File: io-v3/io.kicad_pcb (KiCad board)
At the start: 2 copper layers, 99 parts, among them P1 OUT_GND, P10 INJ-CPU, P11 INJECTORS, P12 LSD-CPU, P13 LSDS, P2 TRIG-cpu, P3 DIG-CPU, P4 IN-CPU, P5 CPU_PWR, P6 TRIG-IN, P7 DIG-IN, P8 IGNITION, P9 PWR_IN, Q1 MOSFET, Q2 MOSFET, Q3 MOSFET, Q4 MOSFET, Q5 MOSFET, Q6 MOSFET, Q7 MOSFET, Q8 MOSFET, U1 LM2940, U12 MIC4469, U13 MIC4469, U2 MIC4469, U3 MAX9926UAEE+

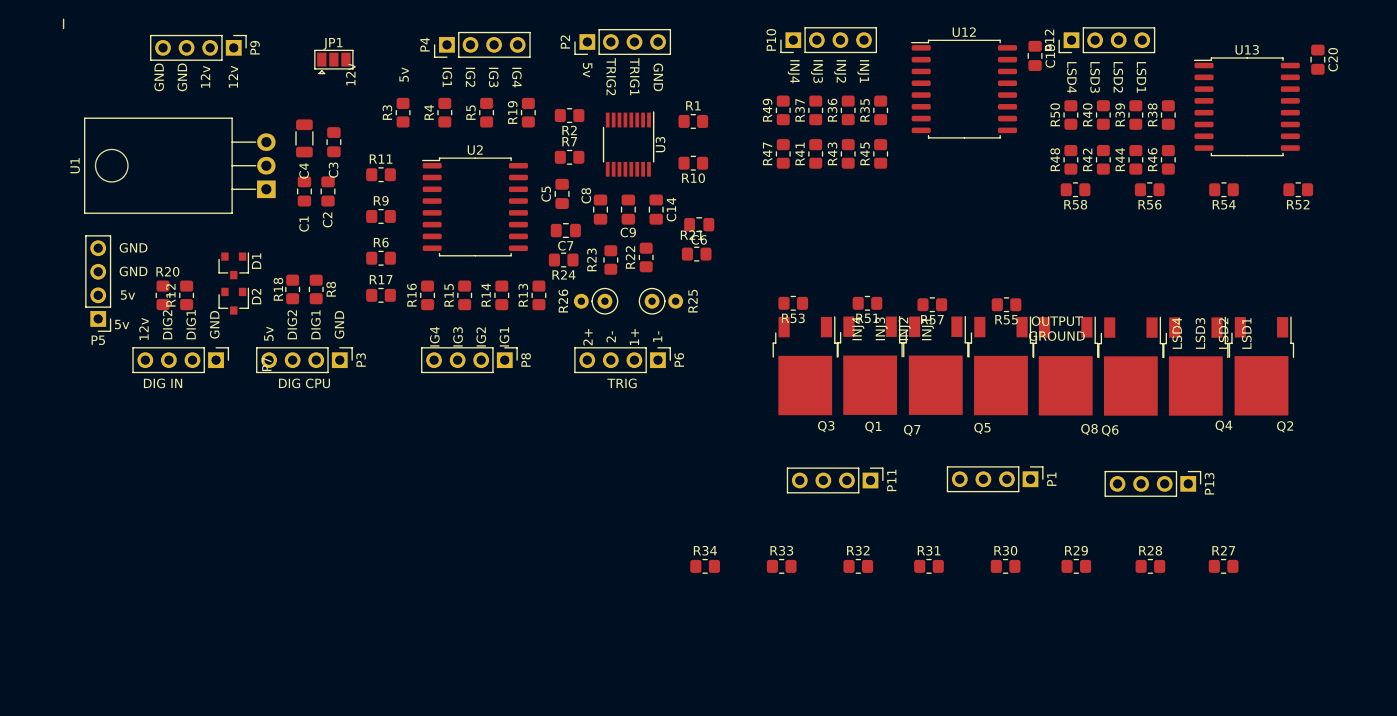
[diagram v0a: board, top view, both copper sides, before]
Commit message: Add LEDs and make a board size
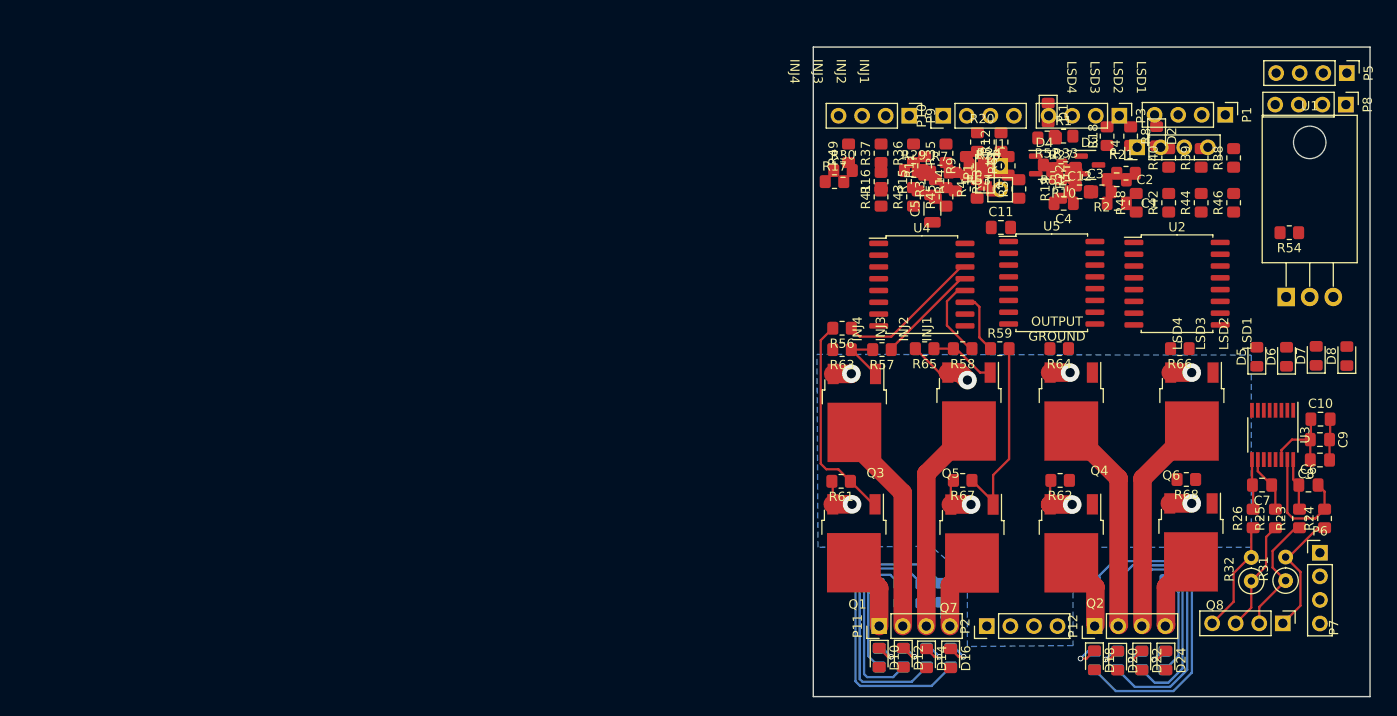
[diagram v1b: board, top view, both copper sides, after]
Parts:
- removed C14: 1u, Capacitor_SMD:C_0805_2012Metric_Pad1.18x1.45mm_HandSolder
- removed C19, C20: 1 uF, Capacitor_SMD:C_0805_2012Metric_Pad1.18x1.45mm_HandSolder
- removed P13: LSDS, Connector_PinHeader_2.54mm:PinHeader_1x04_P2.54mm_Vertical
- removed U12, U13: MIC4469, Package_SO:SOIC-16W_7.5x10.3mm_P1.27mm
- added C10: 1u, Capacitor_SMD:C_0805_2012Metric_Pad1.18x1.45mm_HandSolder, F.Cu at (170.5, 148.6)
- added C11: 1 uF, Capacitor_SMD:C_0805_2012Metric_Pad1.18x1.45mm_HandSolder, F.Cu at (136.0, 127.9)
- added C12: 1 uF, Capacitor_SMD:C_0805_2012Metric_Pad1.18x1.45mm_HandSolder, F.Cu at (144.5, 124.1)
- added D10: LED, LED_SMD:LED_0805_2012Metric_Pad1.15x1.40mm_HandSolder, F.Cu at (122.9, 174.3)
- added D11: 1N4148, Diode_SMD:D_0805_2012Metric_Pad1.15x1.40mm_HandSolder, B.Cu at (125.1, 167.4)
- added D12: LED, LED_SMD:LED_0805_2012Metric_Pad1.15x1.40mm_HandSolder, F.Cu at (125.5, 174.3)
- added D13: 1N4148, Diode_SMD:D_0805_2012Metric_Pad1.15x1.40mm_HandSolder, B.Cu at (127.5, 167.4)
- added D14: LED, LED_SMD:LED_0805_2012Metric_Pad1.15x1.40mm_HandSolder, F.Cu at (128.0, 174.4)
- added D15: 1N4148, Diode_SMD:D_0805_2012Metric_Pad1.15x1.40mm_HandSolder, B.Cu at (129.6, 167.3)
- added D16: LED, LED_SMD:LED_0805_2012Metric_Pad1.15x1.40mm_HandSolder, F.Cu at (130.6, 174.4)
- added D17: 1N4148, Diode_SMD:D_0805_2012Metric_Pad1.15x1.40mm_HandSolder, B.Cu at (146.1, 167.0)
- added D18: LED, LED_SMD:LED_0805_2012Metric_Pad1.15x1.40mm_HandSolder, F.Cu at (146.1, 174.6)
- added D19: 1N4148, Diode_SMD:D_0805_2012Metric_Pad1.15x1.40mm_HandSolder, B.Cu at (148.6, 167.0)
- added D20: LED, LED_SMD:LED_0805_2012Metric_Pad1.15x1.40mm_HandSolder, F.Cu at (148.6, 174.6)
- added D21: 1N4148, Diode_SMD:D_0805_2012Metric_Pad1.15x1.40mm_HandSolder, B.Cu at (151.2, 166.9)
- added D22: LED, LED_SMD:LED_0805_2012Metric_Pad1.15x1.40mm_HandSolder, F.Cu at (151.2, 174.6)
- added D23: 1N4148, Diode_SMD:D_0805_2012Metric_Pad1.15x1.40mm_HandSolder, B.Cu at (153.8, 166.9)
- added D24: LED, LED_SMD:LED_0805_2012Metric_Pad1.15x1.40mm_HandSolder, F.Cu at (153.8, 174.6)
- added D3: BAT54S, Package_TO_SOT_SMD:SOT-23, F.Cu at (145.6, 121.2)
- added D4: BAT54S, Package_TO_SOT_SMD:SOT-23, F.Cu at (140.7, 121.2)
- added D5: LED, LED_SMD:LED_0805_2012Metric_Pad1.15x1.40mm_HandSolder, F.Cu at (163.6, 141.9)
- added D6: LED, LED_SMD:LED_0805_2012Metric_Pad1.15x1.40mm_HandSolder, F.Cu at (166.8, 141.9)
- added D7: LED, LED_SMD:LED_0805_2012Metric_Pad1.15x1.40mm_HandSolder, F.Cu at (170.0, 141.8)
- added D8: LED, LED_SMD:LED_0805_2012Metric_Pad1.15x1.40mm_HandSolder, F.Cu at (173.3, 141.8)
- added D9: 1N4148, Diode_SMD:D_0805_2012Metric_Pad1.15x1.40mm_HandSolder, B.Cu at (122.8, 167.3)
- added J1: DIG-in, Connector_PinHeader_2.54mm:PinHeader_1x02_P2.54mm_Vertical, F.Cu at (135.9, 121.3)
- added R59: 150, Resistor_SMD:R_0805_2012Metric_Pad1.20x1.40mm_HandSolder, F.Cu at (135.9, 141.0)
- added R60: 1k, Resistor_SMD:R_0805_2012Metric_Pad1.20x1.40mm_HandSolder, B.Cu at (130.6, 174.3)
- added R61: 10k, Resistor_SMD:R_0805_2012Metric_Pad1.20x1.40mm_HandSolder, F.Cu at (118.8, 155.3)
- added R62: 10k, Resistor_SMD:R_0805_2012Metric_Pad1.20x1.40mm_HandSolder, F.Cu at (142.4, 155.2)
- added R63: 10k, Resistor_SMD:R_0805_2012Metric_Pad1.20x1.40mm_HandSolder, F.Cu at (118.9, 141.1)
- added R64: 10k, Resistor_SMD:R_0805_2012Metric_Pad1.20x1.40mm_HandSolder, F.Cu at (142.3, 141.0)
- added R65: 10k, Resistor_SMD:R_0805_2012Metric_Pad1.20x1.40mm_HandSolder, F.Cu at (127.8, 141.0)
- added R66: 10k, Resistor_SMD:R_0805_2012Metric_Pad1.20x1.40mm_HandSolder, F.Cu at (155.3, 141.0)
- added R67: 10k, Resistor_SMD:R_0805_2012Metric_Pad1.20x1.40mm_HandSolder, F.Cu at (131.9, 155.2)
- added R68: 10k, Resistor_SMD:R_0805_2012Metric_Pad1.20x1.40mm_HandSolder, F.Cu at (156.0, 155.1)
- added R69: 1k, Resistor_SMD:R_0805_2012Metric_Pad1.20x1.40mm_HandSolder, B.Cu at (146.1, 174.6)
- added R70: 1k, Resistor_SMD:R_0805_2012Metric_Pad1.20x1.40mm_HandSolder, B.Cu at (148.6, 174.6)
- added R71: 1k, Resistor_SMD:R_0805_2012Metric_Pad1.20x1.40mm_HandSolder, B.Cu at (151.2, 174.6)
- added R72: 1k, Resistor_SMD:R_0805_2012Metric_Pad1.20x1.40mm_HandSolder, B.Cu at (153.7, 174.6)
- added U4: MIC4469, Package_SO:SOIC-16W_7.5x10.3mm_P1.27mm, F.Cu at (127.5, 134.1)
- added U5: MIC4469, Package_SO:SOIC-16W_7.5x10.3mm_P1.27mm, F.Cu at (141.5, 133.9)
- C4: value 47 uF -> 1 uF; footprint Capacitor_SMD:C_1206_3216Metric -> Capacitor_SMD:C_0805_2012Metric_Pad1.18x1.45mm_HandSolder
- C5: value 1 uF -> 47 uF; footprint Capacitor_SMD:C_0805_2012Metric_Pad1.18x1.45mm_HandSolder -> Capacitor_SMD:C_1206_3216Metric
- D1, D2: value BAT54S -> LED; footprint Package_TO_SOT_SMD:SOT-23 -> LED_SMD:LED_0805_2012Metric_Pad1.15x1.40mm_HandSolder
- P1: value OUT_GND -> IN-CPU
- P10: value INJ-CPU -> LSD-CPU
- P12: value LSD-CPU -> LSDS
- P2: value TRIG-cpu -> OUT_GND
- P3: value DIG-CPU -> TRIG-cpu
- P4: value IN-CPU -> DIG-CPU
- P6: value TRIG-IN -> IGNITION
- P7: value DIG-IN -> TRIG-IN
- P8: value IGNITION -> PWR_IN
- P9: value PWR_IN -> INJ-CPU
- R10: value 10k -> 1k
- R12: value 1k -> 10k
- R13, R15: value 150 -> 100k
- R14, R16, R33, R34: value 150 -> 1k
- R17, R48: value 100k -> 1k
- R25, R26: value 330 -> 1k; footprint Resistor_THT:R_Axial_DIN0207_L6.3mm_D2.5mm_P2.54mm_Vertical -> Resistor_SMD:R_0805_2012Metric_Pad1.20x1.40mm_HandSolder
- R31, R32: value 150 -> 330; footprint Resistor_SMD:R_0805_2012Metric_Pad1.20x1.40mm_HandSolder -> Resistor_THT:R_Axial_DIN0207_L6.3mm_D2.5mm_P2.54mm_Vertical
- R39, R40: value 1k -> 100k
- R47: value 100k -> 1k; moved to B.Cu
- R50: moved to B.Cu
- R51, R52, R53, R54, R56, R57, R58: value 10k -> 150
- R55: value 10k -> 1k; moved to B.Cu
- R6: value 100k -> 2.4k
- R7: value 10k -> 100k
- R8: value 1k -> 2.4k
- R9: value 100k -> 10k
- moved P5 137.1 mm to (173.3, 111.3), turned to -90 degrees
- moved P7 118.4 mm to (166.4, 170.6)
- moved U1 110.5 mm to (166.8, 135.4), turned to 0 degrees
- moved D2 101.0 mm to (152.8, 118.1)
- moved P8 94.7 mm to (173.2, 114.7)
- moved D1 89.3 mm to (141.1, 115.6)
- moved R12 89.3 mm to (136.0, 118.7)
- moved R18 89.3 mm to (147.5, 118.1)
- moved R20 89.3 mm to (133.5, 118.7)
- moved R8 89.3 mm to (150.0, 118.1)
- moved P3 88.0 mm to (148.8, 115.9)
- moved C1 87.5 mm to (148.5, 125.3), turned to 180 degrees
- moved R24 86.6 mm to (170.9, 159.3), turned to 90 degrees
- moved C2 85.0 mm to (148.5, 122.8), turned to 180 degrees
- moved C4 82.1 mm to (142.8, 125.3), turned to 180 degrees
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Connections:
- C4 pad 1: 5v -> Net-(C4-Pad1)
- C5 pad 1: Net-(C5-Pad1) -> 5v
- D1 pad 1: GND -> Net-(D1-Pad1)
- D2 pad 1: GND -> Net-(D2-Pad1)
- JP1 pad 2: Net-(C5-Pad1) -> Net-(C4-Pad1)
- P1 pad 1: OUT_GND -> IG1-cpu
- P1 pad 2: OUT_GND -> IG2-cpu
- P1 pad 3: OUT_GND -> IG3-cpu
- P1 pad 4: OUT_GND -> IG4-cpu
- P10 pad 1: INJ4-cpu -> LSD4-cpu
- P10 pad 2: INJ3-cpu -> LSD3-cpu
- P10 pad 3: INJ2-cpu -> LSD2-cpu
- P10 pad 4: INJ1-cpu -> LSD1-cpu
- P12 pad 1: LSD4-cpu -> LSD1-out
- P12 pad 2: LSD3-cpu -> LSD2-out
- P12 pad 3: LSD2-cpu -> LSD3-out
- P12 pad 4: LSD1-cpu -> LSD4-out
- P2 pad 1: 5v -> OUT_GND
- P2 pad 2: TRIG2 -> OUT_GND
- P2 pad 3: TRIG1 -> OUT_GND
- P2 pad 4: GND -> OUT_GND
- P3 pad 1: GND -> 5v
- P3 pad 2: DIG1-cpu -> TRIG2
- P3 pad 3: DIG2-cpu -> TRIG1
- P3 pad 4: 5v -> GND
- P4 pad 1: IG1-cpu -> GND
- P4 pad 2: IG2-cpu -> DIG1-cpu
- P4 pad 3: IG3-cpu -> DIG2-cpu
- P4 pad 4: IG4-cpu -> 5v
- P6 pad 1: TRIG1IN- -> IG1-out
- P6 pad 2: TRIG1IN+ -> IG2-out
- P6 pad 3: TRIG2IN- -> IG3-out
- P6 pad 4: TRIG2IN+ -> IG4-out
- P7 pad 1: GND -> TRIG1IN-
- P7 pad 2: DIG1-in -> TRIG1IN+
- P7 pad 3: DIG2-in -> TRIG2IN-
- P7 pad 4: 12v_power -> TRIG2IN+
- P8 pad 1: IG1-out -> 12v_power
- P8 pad 2: IG2-out -> 12v_power
- P8 pad 3: IG3-out -> GND
- P8 pad 4: IG4-out -> GND
- P9 pad 1: 12v_power -> INJ4-cpu
- P9 pad 2: 12v_power -> INJ3-cpu
- P9 pad 3: GND -> INJ2-cpu
- P9 pad 4: GND -> INJ1-cpu
- R10 pad 1: 5v -> Net-(D3-Pad3)
- R10 pad 2: Net-(R1-Pad1) -> DIG1-cpu
- R12 pad 1: DIG1-in -> 5v
- R12 pad 2: Net-(D1-Pad3) -> Net-(R1-Pad1)
- R13 pad 1: IG1-out -> GND
- R14 pad 1: IG2-out -> DIG1-in
- R14 pad 2: Net-(R14-Pad2) -> Net-(D3-Pad3)
- R15 pad 1: IG3-out -> GND
- R16 pad 1: IG4-out -> Net-(D4-Pad3)
- R16 pad 2: Net-(R16-Pad2) -> DIG2-cpu
- R17 pad 1: GND -> Net-(R15-Pad2)
- R17 pad 2: Net-(R17-Pad2) -> IG4-cpu
- R18 pad 1: Net-(D2-Pad3) -> Net-(D5-Pad2)
- R18 pad 2: DIG2-cpu -> Net-(R18-Pad2)
- R19 pad 1: Net-(R17-Pad2) -> DIG2-in
- R19 pad 2: IG4-cpu -> Net-(D4-Pad3)
- R20 pad 1: DIG2-in -> Net-(D6-Pad2)
- R20 pad 2: Net-(D2-Pad3) -> Net-(R20-Pad2)
- R21 pad 1: TRIG1IN+ -> Net-(D7-Pad2)
- R21 pad 2: Net-(C6-Pad1) -> Net-(R21-Pad2)
- R22 pad 1: TRIG1IN- -> Net-(D8-Pad2)
- R22 pad 2: Net-(C6-Pad2) -> Net-(R22-Pad2)
- R23 pad 1: TRIG2IN- -> TRIG1IN+
- R23 pad 2: Net-(C7-Pad1) -> Net-(C6-Pad1)
- R24 pad 1: TRIG2IN+ -> TRIG1IN-
- R24 pad 2: Net-(C7-Pad2) -> Net-(C6-Pad2)
- R25 pad 1: TRIG1IN+ -> TRIG2IN-
- R25 pad 2: TRIG1IN- -> Net-(C7-Pad1)
- R26 pad 1: TRIG2IN- -> TRIG2IN+
- R26 pad 2: TRIG2IN+ -> Net-(C7-Pad2)
- R27 pad 1: Net-(U13-Pad14) -> IG1-out
- R27 pad 2: Net-(Q2-Pad1) -> Net-(R18-Pad2)
- R28 pad 1: Net-(U13-Pad13) -> IG2-out
- R28 pad 2: Net-(Q4-Pad1) -> Net-(R20-Pad2)
- R29 pad 1: Net-(U13-Pad12) -> IG3-out
- R29 pad 2: Net-(Q6-Pad1) -> Net-(R21-Pad2)
- R3 pad 1: Net-(R11-Pad2) -> Net-(R13-Pad2)
- R30 pad 1: Net-(U13-Pad11) -> IG4-out
- R30 pad 2: Net-(Q8-Pad1) -> Net-(R22-Pad2)
- R31 pad 1: Net-(U12-Pad14) -> TRIG1IN+
- R31 pad 2: Net-(Q1-Pad1) -> TRIG1IN-
- R32 pad 1: Net-(U12-Pad13) -> TRIG2IN-
- R32 pad 2: Net-(Q3-Pad1) -> TRIG2IN+
- R33 pad 1: Net-(U12-Pad12) -> Net-(R33-Pad1)
- R33 pad 2: Net-(Q5-Pad1) -> INJ1-cpu
- R34 pad 1: Net-(U12-Pad11) -> Net-(R34-Pad1)
- R34 pad 2: Net-(Q7-Pad1) -> INJ2-cpu
- R35 pad 2: INJ1-cpu -> INJ3-cpu
- R36 pad 2: INJ2-cpu -> LSD1-cpu
- R37 pad 2: INJ3-cpu -> LSD2-cpu
- R38 pad 2: LSD1-cpu -> LSD3-cpu
- R39 pad 1: Net-(R39-Pad1) -> GND
- R39 pad 2: LSD2-cpu -> Net-(R35-Pad1)
- R4 pad 1: Net-(R4-Pad1) -> Net-(R11-Pad2)
- R40 pad 1: Net-(R40-Pad1) -> GND
- R40 pad 2: LSD3-cpu -> Net-(R38-Pad1)
- R41 pad 2: Net-(R37-Pad1) -> Net-(R34-Pad1)
- R42 pad 2: Net-(R40-Pad1) -> Net-(R37-Pad1)
- R43 pad 2: Net-(R36-Pad1) -> Net-(R33-Pad1)
- R44 pad 2: Net-(R39-Pad1) -> Net-(R36-Pad1)
- R45 pad 2: Net-(R35-Pad1) -> Net-(R45-Pad2)
- R46 pad 2: Net-(R38-Pad1) -> Net-(R46-Pad2)
- R47 pad 1: GND -> Net-(R47-Pad1)
- R47 pad 2: Net-(R47-Pad2) -> Net-(D9-Pad2)
- R48 pad 1: GND -> Net-(R45-Pad2)
- R48 pad 2: Net-(R48-Pad2) -> INJ4-cpu
- R49 pad 1: Net-(R47-Pad2) -> Net-(R46-Pad2)
- R49 pad 2: INJ4-cpu -> LSD4-cpu
- R50 pad 1: Net-(R48-Pad2) -> Net-(R50-Pad1)
- R50 pad 2: LSD4-cpu -> Net-(D11-Pad2)
- R51 pad 1: Net-(Q1-Pad1) -> Net-(R51-Pad1)
- R51 pad 2: OUT_GND -> Net-(Q2-Pad1)
- R52 pad 1: Net-(Q2-Pad1) -> Net-(R52-Pad1)
- R52 pad 2: OUT_GND -> Net-(Q4-Pad1)
- R53 pad 1: Net-(Q3-Pad1) -> Net-(R53-Pad1)
- R53 pad 2: OUT_GND -> Net-(Q6-Pad1)
- R54 pad 1: Net-(Q4-Pad1) -> Net-(R54-Pad1)
- R54 pad 2: OUT_GND -> Net-(Q8-Pad1)
- R55 pad 1: Net-(Q5-Pad1) -> Net-(R55-Pad1)
- R55 pad 2: OUT_GND -> Net-(D13-Pad2)
- R56 pad 1: Net-(Q6-Pad1) -> Net-(R56-Pad1)
- R56 pad 2: OUT_GND -> Net-(Q1-Pad1)
- R57 pad 1: Net-(Q7-Pad1) -> Net-(R57-Pad1)
- R57 pad 2: OUT_GND -> Net-(Q3-Pad1)
- R58 pad 1: Net-(Q8-Pad1) -> Net-(R58-Pad1)
- R58 pad 2: OUT_GND -> Net-(Q5-Pad1)
- R6 pad 1: GND -> Net-(D1-Pad1)
- R6 pad 2: Net-(R5-Pad1) -> Net-(R2-Pad1)
- R7 pad 1: 5v -> GND
- R7 pad 2: Net-(R2-Pad1) -> Net-(R5-Pad1)
- R8 pad 1: Net-(D1-Pad3) -> Net-(D2-Pad1)
- R8 pad 2: DIG1-cpu -> Net-(R1-Pad1)
- R9 pad 1: GND -> 5v
- R9 pad 2: Net-(R4-Pad1) -> Net-(R2-Pad1)
- U2 pad 1: Net-(R11-Pad2) -> Net-(R13-Pad2)
- U2 pad 11: Net-(R16-Pad2) -> Net-(R22-Pad2)
- U2 pad 12: Net-(R15-Pad2) -> Net-(R21-Pad2)
- U2 pad 13: Net-(R14-Pad2) -> Net-(R20-Pad2)
- U2 pad 14: Net-(R13-Pad2) -> Net-(R18-Pad2)
- U2 pad 15: Net-(C5-Pad1) -> Net-(C4-Pad1)
- U2 pad 16: Net-(C5-Pad1) -> Net-(C4-Pad1)
- U2 pad 3: Net-(R4-Pad1) -> Net-(R11-Pad2)
- U2 pad 9: Net-(R17-Pad2) -> Net-(R15-Pad2)
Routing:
- net Net-(R69-Pad2): track 0.00 -> 34.8 mm
- net Net-(D15-Pad2): track 0.00 -> 33.4 mm
- net OUT_GND: track 0.00 -> 30.3 mm, vias 0 -> 8
- net Net-(R70-Pad2): track 0.00 -> 27.8 mm
- net Net-(D13-Pad2): track 0.00 -> 26.8 mm
- net LSD3-out: track 0.00 -> 26.2 mm
- net LSD2-out: track 0.00 -> 25.9 mm
- net INJ2-out: track 0.00 -> 25.7 mm
- net INJ3-out: track 0.00 -> 25.6 mm
- net Net-(Q1-Pad1): track 0.00 -> 22.8 mm
- net Net-(Q7-Pad1): track 0.00 -> 21.1 mm
- net Net-(R71-Pad2): track 0.00 -> 20.5 mm
- net Net-(D11-Pad2): track 0.00 -> 19.5 mm
- net Net-(R56-Pad1): track 0.00 -> 15.7 mm
- net TRIG1IN-: track 0.00 -> 14.1 mm
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- added copper zone on B.Cu, net OUT_GND
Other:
- board outline added: 60 x 70 mm
- board text removed: "1+"
- board text removed: "1-"
- board text removed: "12v"
- board text removed: "2+"
- board text removed: "2-"
- board text removed: "5v"
- board text removed: "DIG CPU"
- board text removed: "DIG IN"
- board text removed: "DIG1"
- board text removed: "DIG2"
- board text removed: "GND"
- board text removed: "IG1"
- board text removed: "IG2"
- board text removed: "IG3"
- board text removed: "IG4"
- board text removed: "TRIG"
- board text removed: "TRIG1"
- board text removed: "TRIG2"

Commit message: Rework IO board to just be an LSD breakout board
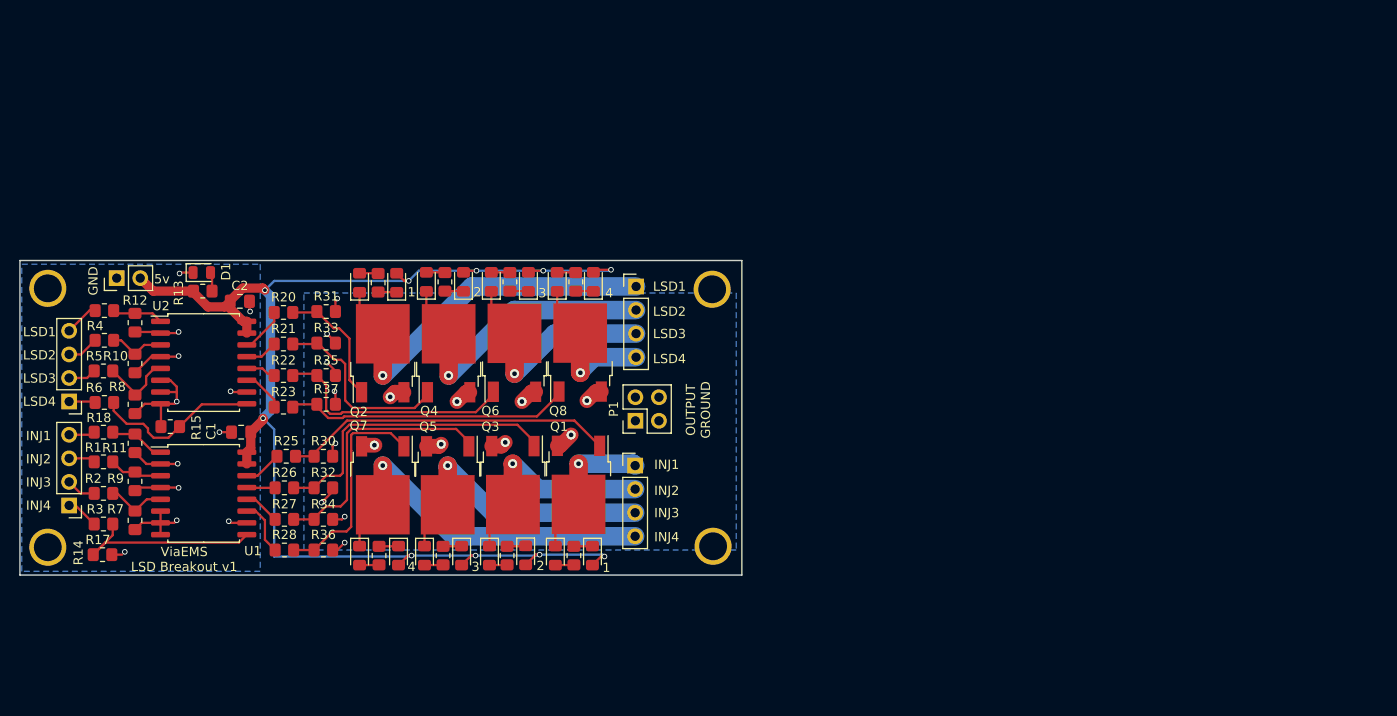
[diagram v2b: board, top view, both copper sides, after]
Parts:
- removed C10: 1u, Capacitor_SMD:C_0805_2012Metric_Pad1.18x1.45mm_HandSolder
- removed C11, C12, C4: 1 uF, Capacitor_SMD:C_0805_2012Metric_Pad1.18x1.45mm_HandSolder
- removed C3: 0.1 uF, Capacitor_SMD:C_0805_2012Metric_Pad1.18x1.45mm_HandSolder
- removed C5: 47 uF, Capacitor_SMD:C_1206_3216Metric
- removed C6, C7: 1n, Capacitor_SMD:C_0805_2012Metric_Pad1.18x1.45mm_HandSolder
- removed C8: 10n, Capacitor_SMD:C_0805_2012Metric_Pad1.18x1.45mm_HandSolder
- removed C9: 0.1u, Capacitor_SMD:C_0805_2012Metric_Pad1.18x1.45mm_HandSolder
- removed D18, D20, D22, D24: LED, LED_SMD:LED_0805_2012Metric_Pad1.15x1.40mm_HandSolder
- removed D19, D21, D23: 1N4148, Diode_SMD:D_0805_2012Metric_Pad1.15x1.40mm_HandSolder
- removed J1: DIG-in, Connector_PinHeader_2.54mm:PinHeader_1x02_P2.54mm_Vertical
- removed JP1: IG_PWR, Jumper:SolderJumper-3_P1.3mm_Open_Pad1.0x1.5mm
- removed P10: LSD-CPU, Connector_PinHeader_2.54mm:PinHeader_1x04_P2.54mm_Vertical
- removed P11: INJECTORS, Connector_PinHeader_2.54mm:PinHeader_1x04_P2.54mm_Vertical
- removed P12: LSDS, Connector_PinHeader_2.54mm:PinHeader_1x04_P2.54mm_Vertical
- removed P7: TRIG-IN, Connector_PinHeader_2.54mm:PinHeader_1x04_P2.54mm_Vertical
- removed P8: PWR_IN, Connector_PinHeader_2.54mm:PinHeader_1x04_P2.54mm_Vertical
- removed P9: INJ-CPU, Connector_PinHeader_2.54mm:PinHeader_1x04_P2.54mm_Vertical
- removed R42, R43, R44, R45, R46: 100k, Resistor_SMD:R_0805_2012Metric_Pad1.20x1.40mm_HandSolder
- removed R47, R48, R49, R50, R55, R60, R69, R70, R71, R72: 1k, Resistor_SMD:R_0805_2012Metric_Pad1.20x1.40mm_HandSolder
- removed R51, R52, R53, R54, R56, R57, R58, R59: 150, Resistor_SMD:R_0805_2012Metric_Pad1.20x1.40mm_HandSolder
- removed R61, R62, R63, R64, R65, R66, R67, R68: 10k, Resistor_SMD:R_0805_2012Metric_Pad1.20x1.40mm_HandSolder
- removed U3: MAX9926UAEE+, Package_SO:QSOP-16_3.9x4.9mm_P0.635mm
- removed U4, U5: MIC4469, Package_SO:SOIC-16W_7.5x10.3mm_P1.27mm
- added REF**: MountingHole_2.5mm_Pad, MountingHole:MountingHole_2.5mm_Pad, F.Cu at (104.9, 134.6)
- added REF**: MountingHole_2.5mm_Pad, MountingHole:MountingHole_2.5mm_Pad, F.Cu at (105.0, 162.3)
- added REF**: MountingHole_2.5mm_Pad, MountingHole:MountingHole_2.5mm_Pad, F.Cu at (33.3, 134.5)
- added REF**: MountingHole_2.5mm_Pad, MountingHole:MountingHole_2.5mm_Pad, F.Cu at (33.3, 162.4)
- C1: value 10 uF -> 1 uF
- C2: value 0.1 uF -> 1 uF
- D1: footprint LED_SMD:LED_0805_2012Metric_Pad1.15x1.40mm_HandSolder -> LED_SMD:LED_0805_2012Metric
- D10, D12, D14, D16, D2, D6, D8: value LED -> 1N4148; footprint LED_SMD:LED_0805_2012Metric_Pad1.15x1.40mm_HandSolder -> Diode_SMD:D_0805_2012Metric_Pad1.15x1.40mm_HandSolder
- D11, D13, D15, D17, D9: value 1N4148 -> LED; footprint Diode_SMD:D_0805_2012Metric_Pad1.15x1.40mm_HandSolder -> LED_SMD:LED_0805_2012Metric_Pad1.15x1.40mm_HandSolder; moved to F.Cu
- D3: value BAT54S -> LED; footprint Package_TO_SOT_SMD:SOT-23 -> LED_SMD:LED_0805_2012Metric_Pad1.15x1.40mm_HandSolder
- D4: value BAT54S -> 1N4148; footprint Package_TO_SOT_SMD:SOT-23 -> Diode_SMD:D_0805_2012Metric_Pad1.15x1.40mm_HandSolder
- P1: value IN-CPU -> GND; footprint Connector_PinHeader_2.54mm:PinHeader_1x04_P2.54mm_Vertical -> Connector_PinHeader_2.54mm:PinHeader_2x02_P2.54mm_Vertical
- P2: value OUT_GND -> INJ-CPU
- P3: value TRIG-cpu -> LSD-CPU
- P4: value DIG-CPU -> POWER; footprint Connector_PinHeader_2.54mm:PinHeader_1x04_P2.54mm_Vertical -> Connector_PinHeader_2.54mm:PinHeader_1x02_P2.54mm_Vertical
- P5: value CPU_PWR -> INJECTORS
- P6: value IGNITION -> LSDS
- R10, R14: value 1k -> 100k
- R12, R9: value 10k -> 100k
- R13: value 100k -> 2.4k
- R20, R21, R22, R23, R25, R26: value 1k -> 150
- R29: value 150 -> 1k
- R30: value 150 -> 10k
- R31, R32: value 330 -> 10k; footprint Resistor_THT:R_Axial_DIN0207_L6.3mm_D2.5mm_P2.54mm_Vertical -> Resistor_SMD:R_0805_2012Metric_Pad1.20x1.40mm_HandSolder
- R33, R34, R35, R36, R37: value 1k -> 10k
- R39, R40, R41: value 100k -> 1k
- R6: value 2.4k -> 1k
- R8: value 2.4k -> 100k
- U1: value LM2940 -> MIC4469; footprint Package_TO_SOT_THT:TO-220-3_Horizontal_TabDown -> Package_SO:SOIC-16W_7.5x10.3mm_P1.27mm
- moved U1 118.6 mm to (50.1, 156.6)
- moved P3 117.3 mm to (35.6, 146.7), turned to 180 degrees
- moved R18 111.8 mm to (39.4, 146.8), turned to 180 degrees
- moved R2 111.5 mm to (39.3, 153.2)
- moved R8 111.1 mm to (42.7, 147.0), turned to 90 degrees
- moved P4 110.9 mm to (40.7, 133.4)
- moved R23 110.2 mm to (58.7, 147.3), turned to 0 degrees
- moved D8 108.6 mm to (66.9, 163.3), turned to -90 degrees
- moved R1 108.3 mm to (39.3, 150.0), turned to 180 degrees
- moved R31 107.4 mm to (63.3, 137.0), turned to 0 degrees
- moved R25 106.8 mm to (59.0, 152.6), turned to 0 degrees
- moved U2 105.2 mm to (50.1, 142.5)
- moved R26 104.5 mm to (58.8, 156.0), turned to 0 degrees
- moved R10 102.1 mm to (42.7, 142.6), turned to 90 degrees
- moved R32 100.5 mm to (63.0, 156.0), turned to 0 degrees
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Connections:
- C1 pad 1: 12v_power -> 5v
- C2 pad 1: 12v_power -> 5v
- D1 pad 1: Net-(D1-Pad1) -> GND
- D1 pad 2: 5v -> Net-(D1-Pad2)
- D10 pad 1: Net-(R47-Pad1) -> LSD1-out
- D10 pad 2: 5v -> Net-(D10-Pad2)
- D11 pad 1: INJ2-out -> Net-(D11-Pad1)
- D11 pad 2: Net-(D11-Pad2) -> 5v
- D12 pad 1: Net-(R50-Pad1) -> LSD2-out
- D12 pad 2: 5v -> Net-(D12-Pad2)
- D13 pad 1: INJ3-out -> Net-(D13-Pad1)
- D13 pad 2: Net-(D13-Pad2) -> 5v
- D14 pad 1: Net-(R55-Pad1) -> LSD3-out
- D14 pad 2: 5v -> Net-(D14-Pad2)
- D15 pad 1: INJ4-out -> Net-(D15-Pad1)
- D15 pad 2: Net-(D15-Pad2) -> 5v
- D16 pad 1: Net-(R60-Pad1) -> LSD4-out
- D16 pad 2: 5v -> Net-(D16-Pad2)
- D17 pad 1: LSD1-out -> Net-(D17-Pad1)
- D17 pad 2: Net-(R69-Pad2) -> 5v
- D2 pad 1: Net-(D2-Pad1) -> INJ1-out
- D2 pad 2: 5v -> Net-(D2-Pad2)
- D3 pad 1: GND -> Net-(D3-Pad1)
- D4 pad 1: GND -> INJ2-out
- D4 pad 2: 5v -> Net-(D4-Pad2)
- D5 pad 1: GND -> Net-(D5-Pad1)
- D5 pad 2: Net-(D5-Pad2) -> 5v
- D6 pad 1: GND -> INJ3-out
- D7 pad 1: GND -> Net-(D7-Pad1)
- D7 pad 2: Net-(D7-Pad2) -> 5v
- D8 pad 1: GND -> INJ4-out
- D9 pad 1: INJ1-out -> Net-(D9-Pad1)
- D9 pad 2: Net-(D9-Pad2) -> 5v
- P1 pad 1: IG1-cpu -> OUT_GND
- P1 pad 2: IG2-cpu -> OUT_GND
- P1 pad 3: IG3-cpu -> OUT_GND
- P1 pad 4: IG4-cpu -> OUT_GND
- P2 pad 1: OUT_GND -> INJ4-cpu
- P2 pad 2: OUT_GND -> INJ3-cpu
- P2 pad 3: OUT_GND -> INJ2-cpu
- P2 pad 4: OUT_GND -> INJ1-cpu
- P3 pad 1: 5v -> LSD4-cpu
- P3 pad 2: TRIG2 -> LSD3-cpu
- P3 pad 3: TRIG1 -> LSD2-cpu
- P3 pad 4: GND -> LSD1-cpu
- P4 pad 2: DIG1-cpu -> 5v
- P5 pad 1: 5v -> INJ1-out
- P5 pad 2: 5v -> INJ2-out
- P5 pad 3: GND -> INJ3-out
- P5 pad 4: GND -> INJ4-out
- P6 pad 1: IG1-out -> LSD1-out
- P6 pad 2: IG2-out -> LSD2-out
- P6 pad 3: IG3-out -> LSD3-out
- P6 pad 4: IG4-out -> LSD4-out
- R1 pad 2: TRIG1 -> INJ1-cpu
- R10 pad 1: Net-(D3-Pad3) -> GND
- R10 pad 2: DIG1-cpu -> Net-(R5-Pad1)
- R11 pad 2: Net-(R11-Pad2) -> Net-(R1-Pad1)
- R12 pad 1: 5v -> GND
- R12 pad 2: Net-(R1-Pad1) -> Net-(R4-Pad1)
- R13 pad 1: GND -> 5v
- R13 pad 2: Net-(R13-Pad2) -> Net-(D1-Pad2)
- R14 pad 1: DIG1-in -> GND
- R14 pad 2: Net-(D3-Pad3) -> Net-(R14-Pad2)
- R15 pad 2: Net-(R15-Pad2) -> Net-(R18-Pad1)
- R16 pad 1: Net-(D4-Pad3) -> Net-(D3-Pad1)
- R16 pad 2: DIG2-cpu -> Net-(D2-Pad2)
- R17 pad 1: Net-(R15-Pad2) -> Net-(R14-Pad2)
- R17 pad 2: IG4-cpu -> INJ4-cpu
- R18 pad 1: Net-(D5-Pad2) -> Net-(R18-Pad1)
- R18 pad 2: Net-(R18-Pad2) -> LSD4-cpu
- R19 pad 1: DIG2-in -> Net-(D5-Pad1)
- R19 pad 2: Net-(D4-Pad3) -> Net-(D4-Pad2)
- R2 pad 2: TRIG2 -> INJ2-cpu
- R20 pad 1: Net-(D6-Pad2) -> Net-(R20-Pad1)
- R20 pad 2: Net-(R20-Pad2) -> Net-(Q2-Pad1)
- R21 pad 1: Net-(D7-Pad2) -> Net-(R21-Pad1)
- R21 pad 2: Net-(R21-Pad2) -> Net-(Q4-Pad1)
- R22 pad 1: Net-(D8-Pad2) -> Net-(R22-Pad1)
- R22 pad 2: Net-(R22-Pad2) -> Net-(Q6-Pad1)
- R23 pad 1: TRIG1IN+ -> Net-(R23-Pad1)
- R23 pad 2: Net-(C6-Pad1) -> Net-(Q8-Pad1)
- R24 pad 1: TRIG1IN- -> Net-(D7-Pad1)
- R24 pad 2: Net-(C6-Pad2) -> Net-(D6-Pad2)
- R25 pad 1: TRIG2IN- -> Net-(R25-Pad1)
- R25 pad 2: Net-(C7-Pad1) -> Net-(Q1-Pad1)
- R26 pad 1: TRIG2IN+ -> Net-(R26-Pad1)
- R26 pad 2: Net-(C7-Pad2) -> Net-(Q3-Pad1)
- R27 pad 1: IG1-out -> Net-(R27-Pad1)
- R27 pad 2: Net-(R18-Pad2) -> Net-(Q5-Pad1)
- R28 pad 1: IG2-out -> Net-(R28-Pad1)
- R28 pad 2: Net-(R20-Pad2) -> Net-(Q7-Pad1)
- R29 pad 1: IG3-out -> Net-(D9-Pad1)
- R29 pad 2: Net-(R21-Pad2) -> Net-(D8-Pad2)
- R3 pad 1: Net-(R13-Pad2) -> Net-(R3-Pad1)
- R3 pad 2: IG1-cpu -> INJ3-cpu
- R30 pad 1: IG4-out -> Net-(Q1-Pad1)
- R30 pad 2: Net-(R22-Pad2) -> OUT_GND
- R31 pad 1: TRIG1IN+ -> Net-(Q2-Pad1)
- R31 pad 2: TRIG1IN- -> OUT_GND
- R32 pad 1: TRIG2IN- -> Net-(Q3-Pad1)
- R32 pad 2: TRIG2IN+ -> OUT_GND
- R33 pad 1: Net-(R33-Pad1) -> Net-(Q4-Pad1)
- R33 pad 2: INJ1-cpu -> OUT_GND
- R34 pad 1: Net-(R34-Pad1) -> Net-(Q5-Pad1)
- R34 pad 2: INJ2-cpu -> OUT_GND
- R35 pad 1: Net-(R35-Pad1) -> Net-(Q6-Pad1)
- R35 pad 2: INJ3-cpu -> OUT_GND
- R36 pad 1: Net-(R36-Pad1) -> Net-(Q7-Pad1)
- R36 pad 2: LSD1-cpu -> OUT_GND
- R37 pad 1: Net-(R37-Pad1) -> Net-(Q8-Pad1)
- R37 pad 2: LSD2-cpu -> OUT_GND
- R38 pad 1: Net-(R38-Pad1) -> Net-(D11-Pad1)
- R38 pad 2: LSD3-cpu -> Net-(D10-Pad2)
- R39 pad 1: GND -> Net-(D13-Pad1)
- R39 pad 2: Net-(R35-Pad1) -> Net-(D12-Pad2)
- R4 pad 1: Net-(R11-Pad2) -> Net-(R4-Pad1)
- R4 pad 2: IG2-cpu -> LSD1-cpu
- R40 pad 1: GND -> Net-(D15-Pad1)
- R40 pad 2: Net-(R38-Pad1) -> Net-(D14-Pad2)
- R41 pad 1: GND -> Net-(D17-Pad1)
- R41 pad 2: Net-(R34-Pad1) -> Net-(D16-Pad2)
- R5 pad 2: IG3-cpu -> LSD2-cpu
- R6 pad 1: Net-(D1-Pad1) -> Net-(R6-Pad1)
- R6 pad 2: Net-(R2-Pad1) -> LSD3-cpu
- R7 pad 2: Net-(R5-Pad1) -> Net-(R3-Pad1)
- R8 pad 1: Net-(D2-Pad1) -> GND
- R8 pad 2: Net-(R1-Pad1) -> Net-(R6-Pad1)
- R9 pad 1: 5v -> GND
- U1 pad 1: 12v_power -> Net-(R1-Pad1)
- U1 pad 3: 5v -> Net-(R2-Pad1)
- U2 pad 1: Net-(R13-Pad2) -> Net-(R4-Pad1)
- U2 pad 11: Net-(R22-Pad2) -> Net-(R23-Pad1)
- U2 pad 12: Net-(R21-Pad2) -> Net-(R22-Pad1)
- U2 pad 13: Net-(R20-Pad2) -> Net-(R21-Pad1)
- U2 pad 14: Net-(R18-Pad2) -> Net-(R20-Pad1)
- U2 pad 15: Net-(C4-Pad1) -> 5v
- U2 pad 16: Net-(C4-Pad1) -> 5v
- U2 pad 3: Net-(R11-Pad2) -> Net-(R5-Pad1)
- U2 pad 5: Net-(R5-Pad1) -> Net-(R6-Pad1)
- U2 pad 9: Net-(R15-Pad2) -> Net-(R18-Pad1)
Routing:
- net 5v: track 9.03 -> 142.9 mm, vias 0 -> 10
- net GND: track 4.43 -> 48.7 mm, vias 0 -> 12
- net Net-(R69-Pad2): track 34.8 -> 0.00 mm
- net Net-(D15-Pad2): track 33.4 -> 0.00 mm
- net Net-(Q8-Pad1): track 0.00 -> 30.5 mm
- net Net-(R70-Pad2): track 27.8 -> 0.00 mm
- net LSD1-out: track 10.7 -> 37.8 mm, vias 0 -> 1
- net Net-(D13-Pad2): track 26.8 -> 0.00 mm
- net Net-(Q3-Pad1): track 6.00 -> 32.1 mm
- net Net-(Q6-Pad1): track 0.00 -> 25.9 mm
- net INJ4-out: track 10.7 -> 36.5 mm, vias 0 -> 1
- net Net-(R14-Pad2): track 0.00 -> 21.6 mm
- net Net-(R71-Pad2): track 20.5 -> 0.00 mm
- net Net-(Q5-Pad1): track 7.12 -> 27.5 mm
- net Net-(Q4-Pad1): track 0.00 -> 20.1 mm
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- added copper zone on B.Cu, net GND
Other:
- board size 60 x 70 mm -> 77.8 x 33.9 mm
- board text added: "1"
- board text added: "2"
- board text added: "3"
- board text added: "4"
- board text added: "5v"
- board text added: "GND"
- board text added: "ViaEMS LSD Breakout v1"
